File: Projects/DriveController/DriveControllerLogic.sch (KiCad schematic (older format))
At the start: 34 parts, among them U1 ATMega32M1, U2 MCP2562, U3 ATA6844, U4 ACS710

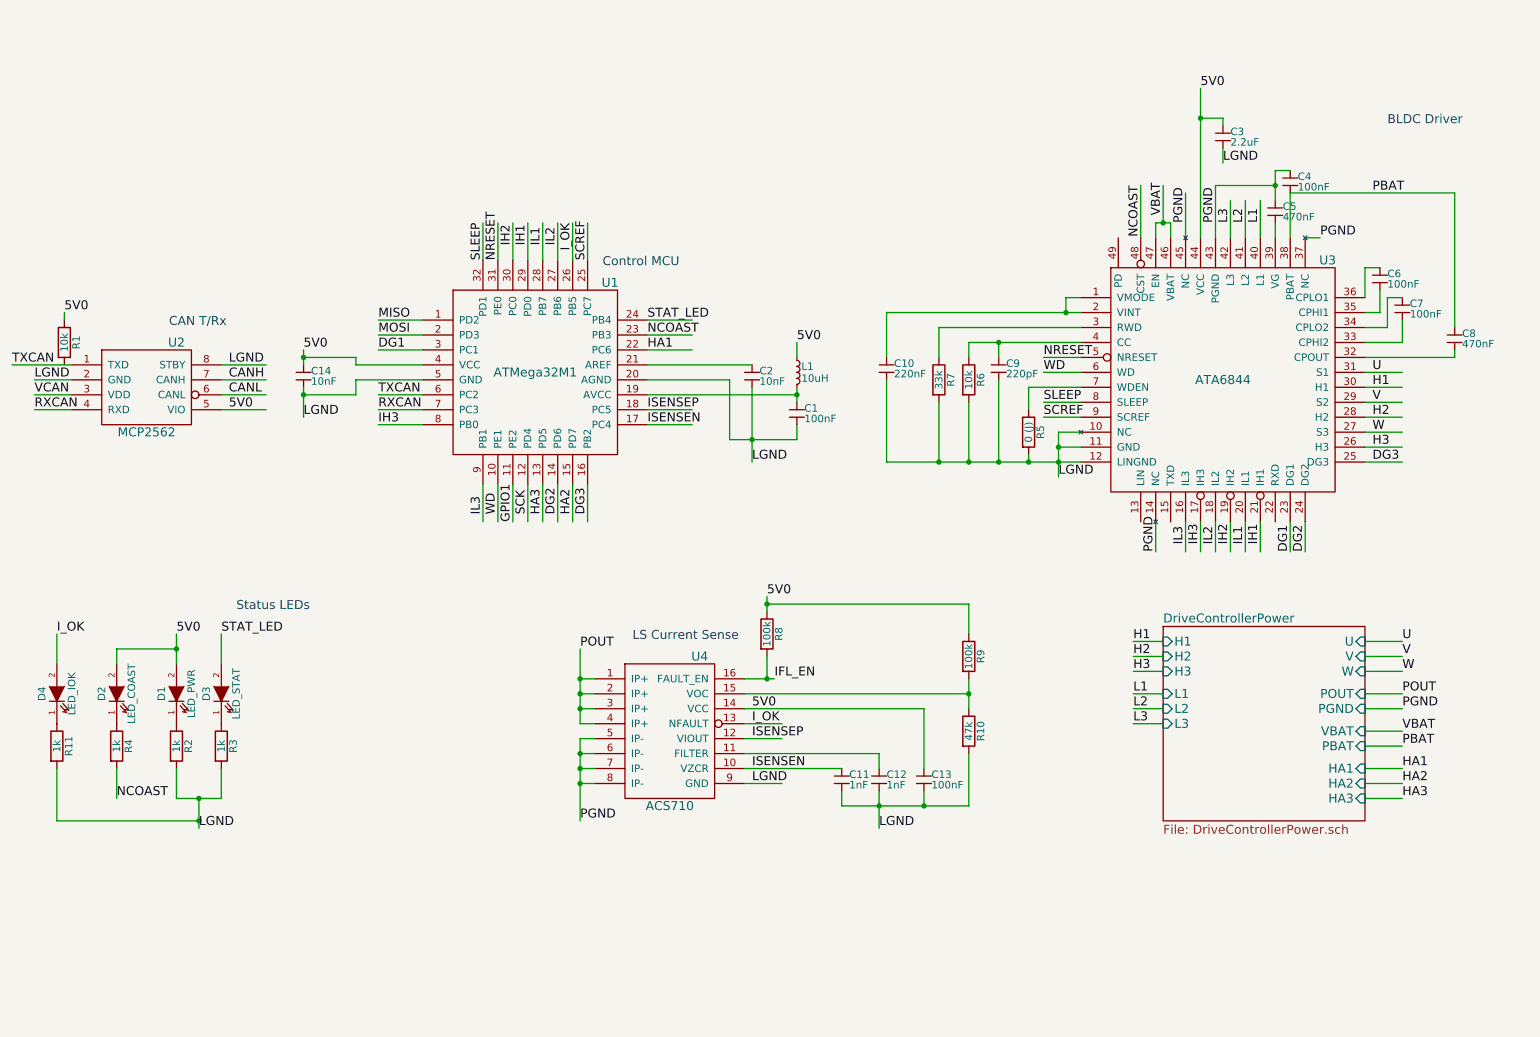
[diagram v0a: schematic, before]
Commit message: Nearly done module schematics
ToDo: Make the footprints for custom parts and layout!
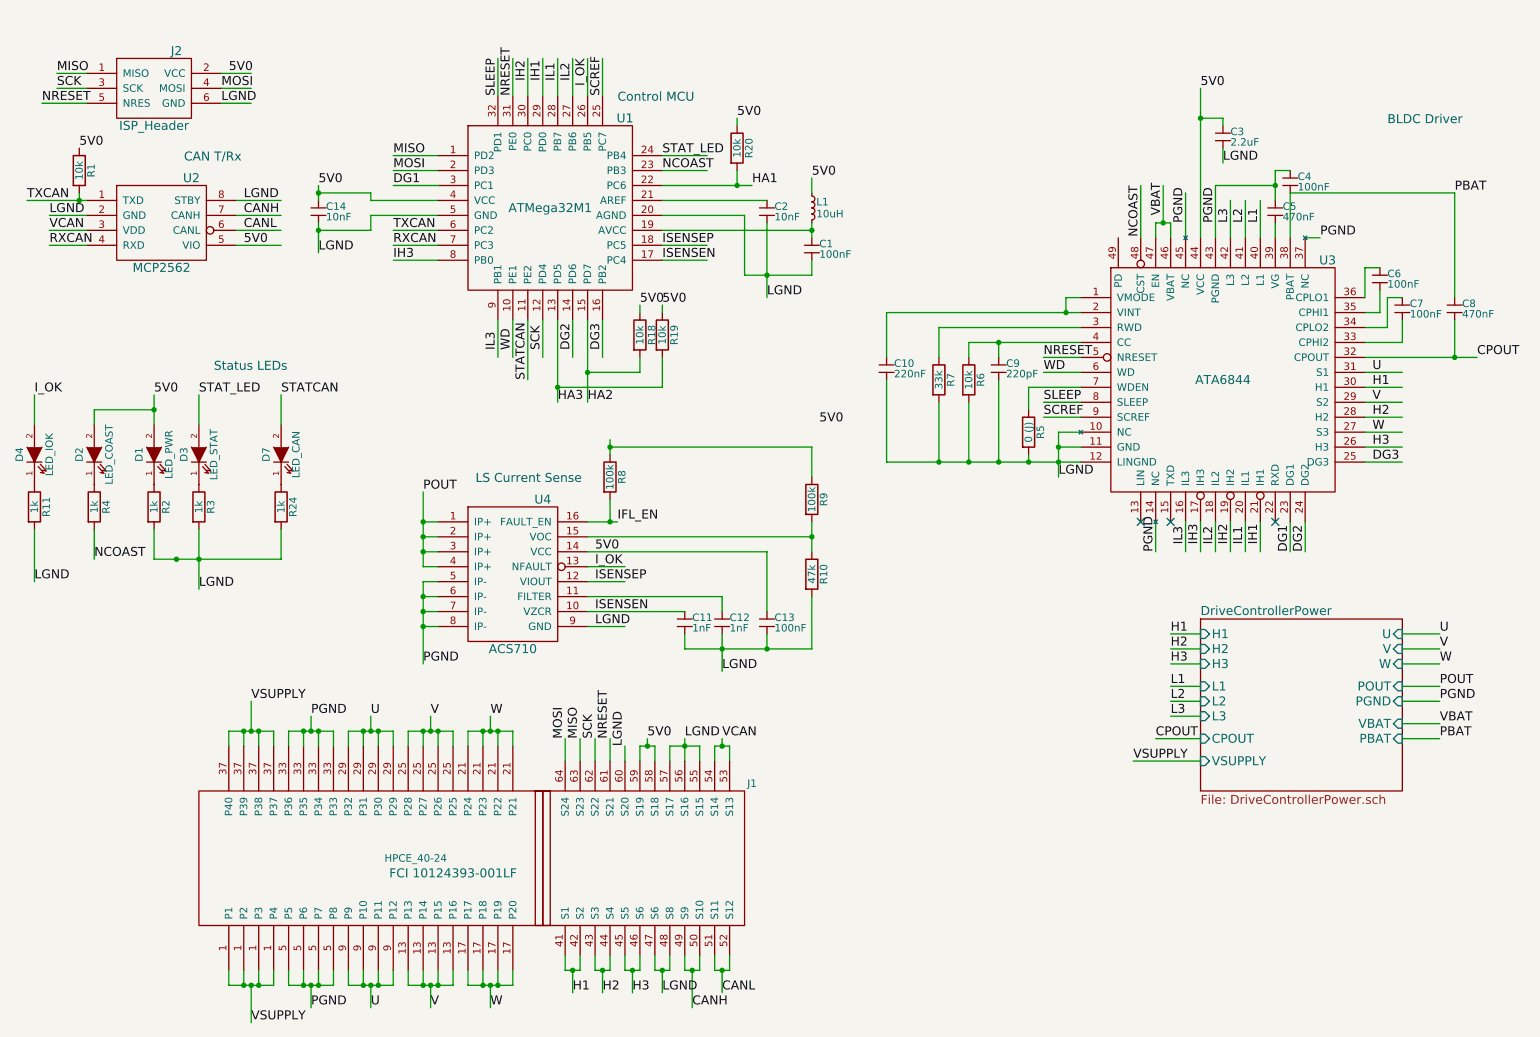
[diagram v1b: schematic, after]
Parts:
- added D7: LED_CAN, symbol LED
- added J1: HPCE_40-24, MODULE, symbol HPCE_40-24
- added J2: ISP_Header, symbol ISP_Header
- added R18, R19, R20: 10k, symbol R
- added R24: 1k, symbol R
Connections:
- net labels added: CPOUT, STATCAN, VSUPPLY
- net labels removed: GPIO1
- wire segments 184 -> 299
- no-connect marks 0 -> 3
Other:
- moved on the sheet: C1, C11, C12, C13, C14, C2, C8, D1, D2, D3, D4, L1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

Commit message: Basic PCB layout organization
No traces yet!
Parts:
- C1, C10, C11, C12, C13, C14, C2, C3, C4, C5, C6, C7, C8, C9, L1: footprint (none) -> Capacitors_SMD:C_0805
- D1, D2, D3, D4, D7: footprint (none) -> LEDs:LED-0805
- J1: footprint MODULE -> USSTPARTS:HPCE-40-24
- J2: footprint (none) -> Pin_Headers:Pin_Header_Straight_2x03
- R1, R10, R11, R18, R19, R2, R20, R24, R3, R4, R5, R6, R7, R8, R9: footprint (none) -> Resistors_SMD:R_0805
- U1: footprint (none) -> Housings_QFP:TQFP-32_7x7mm_Pitch0.8mm
- U2: footprint (none) -> Housings_SOIC:SOIC-8_3.9x4.9mm_Pitch1.27mm
- U3: footprint (none) -> Housings_DFN_QFN:QFN-48-1EP_7x7mm_Pitch0.5mm
- U4: footprint (none) -> Housings_SOIC:SOIC-16_7.5x10.3mm_Pitch1.27mm
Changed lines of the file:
@@
 F 0 "U2" H 1800 2300 60  0000 C CNN
 F 1 "MCP2562" H 1600 1700 60  0000 C CNN
-F 2 "" H 1350 1900 60  0000 C CNN
+F 2 "Housings_SOIC:SOIC-8_3.9x4.9mm_Pitch1.27mm" H 1350 1900 60  0001 C CNN
 F 3 "" H 1350 1900 60  0000 C CNN
 	1    1600 2000
@@
 F 0 "U3" H 9400 3850 60  0000 C CNN
 F 1 "ATA6844" H 8700 3050 60  0000 C CNN
-F 2 "" H 7950 3500 60  0000 C CNN
+F 2 "Housings_DFN_QFN:QFN-48-1EP_7x7mm_Pitch0.5mm" H 7950 3500 60  0001 C CNN
 F 3 "" H 7950 3500 60  0000 C CNN
 	1    8700 3050
@@
 F 0 "U4" H 4150 4850 60  0000 C CNN
 F 1 "ACS710" H 3950 3850 60  0000 C CNN
-F 2 "" H 3650 4350 60  0000 C CNN
+F 2 "Housings_SOIC:SOIC-16_7.5x10.3mm_Pitch1.27mm" H 3650 4350 60  0001 C CNN
 F 3 "" H 3650 4350 60  0000 C CNN
 	1    3950 4350
@@
 F 0 "R1" V 1130 1650 50  0000 C CNN
 F 1 "10k" V 1050 1650 50  0000 C CNN
-F 2 "" V 980 1650 30  0000 C CNN
+F 2 "Resistors_SMD:R_0805" V 980 1650 30  0001 C CNN
 F 3 "" H 1050 1650 30  0000 C CNN
 	1    1050 1650
@@
 F 0 "U1" H 4700 2000 60  0000 C CNN
 F 1 "ATMega32M1" H 4200 1400 60  0000 C CNN
-F 2 "" H 4600 1550 60  0000 C CNN
+F 2 "Housings_QFP:TQFP-32_7x7mm_Pitch0.8mm" H 4600 1550 60  0001 C CNN
 F 3 "" H 4600 1550 60  0000 C CNN
 	1    4500 1650
@@
 F 0 "C2" H 5700 1910 50  0000 L CNN
 F 1 "10nF" H 5700 1840 50  0000 L CNN
-F 2 "" H 5650 1900 60  0000 C CNN
+F 2 "Capacitors_SMD:C_0805" H 5650 1900 60  0001 C CNN
 F 3 "" H 5650 1900 60  0000 C CNN
 	1    5650 1900
@@
 F 0 "C1" H 6000 2160 50  0000 L CNN
 F 1 "100nF" H 6000 2090 50  0000 L CNN
-F 2 "" H 5950 2150 60  0000 C CNN
+F 2 "Capacitors_SMD:C_0805" H 5950 2150 60  0001 C CNN
 F 3 "" H 5950 2150 60  0000 C CNN
 	1    5950 2150
@@
 F 0 "L1" H 5980 1940 50  0000 L CNN
 F 1 "10uH" H 5980 1860 50  0000 L CNN
-F 2 "" H 5950 1900 60  0000 C CNN
+F 2 "Capacitors_SMD:C_0805" H 5950 1900 60  0001 C CNN
 F 3 "" H 5950 1900 60  0000 C CNN
 	1    5950 1900
@@
 F 0 "C14" H 2700 1910 50  0000 L CNN
 F 1 "10nF" H 2700 1840 50  0000 L CNN
-F 2 "" H 2650 1900 60  0000 C CNN
+F 2 "Capacitors_SMD:C_0805" H 2650 1900 60  0001 C CNN
 F 3 "" H 2650 1900 60  0000 C CNN
 	1    2650 1900
@@
 F 0 "D1" H 1550 3650 50  0000 C CNN
 F 1 "LED_PWR" H 1550 3450 50  0000 C CNN
-F 2 "" H 1550 3550 60  0000 C CNN
+F 2 "LEDs:LED-0805" H 1550 3550 60  0001 C CNN
 F 3 "" H 1550 3550 60  0000 C CNN
 	1    1550 3550
@@
 F 0 "D3" H 1850 3650 50  0000 C CNN
 F 1 "LED_STAT" H 1850 3450 50  0000 C CNN
-F 2 "" H 1850 3550 60  0000 C CNN
+F 2 "LEDs:LED-0805" H 1850 3550 60  0001 C CNN
 F 3 "" H 1850 3550 60  0000 C CNN
 	1    1850 3550
@@
 F 0 "R3" V 1930 3900 50  0000 C CNN
 F 1 "1k" V 1850 3900 50  0000 C CNN
-F 2 "" V 1780 3900 30  0000 C CNN
+F 2 "Resistors_SMD:R_0805" V 1780 3900 30  0001 C CNN
 F 3 "" H 1850 3900 30  0000 C CNN
 	1    1850 3900
@@
 F 0 "R2" V 1630 3900 50  0000 C CNN
 F 1 "1k" V 1550 3900 50  0000 C CNN
-F 2 "" V 1480 3900 30  0000 C CNN
+F 2 "Resistors_SMD:R_0805" V 1480 3900 30  0001 C CNN
 F 3 "" H 1550 3900 30  0000 C CNN
 	1    1550 3900
@@
 F 0 "R4" V 1230 3900 50  0000 C CNN
 F 1 "1k" V 1150 3900 50  0000 C CNN
-F 2 "" V 1080 3900 30  0000 C CNN
+F 2 "Resistors_SMD:R_0805" V 1080 3900 30  0001 C CNN
 F 3 "" H 1150 3900 30  0000 C CNN
 	1    1150 3900
@@
 F 0 "D2" H 1150 3650 50  0000 C CNN
 F 1 "LED_COAST" H 1150 3450 50  0000 C CNN
-F 2 "" H 1150 3550 60  0000 C CNN
+F 2 "LEDs:LED-0805" H 1150 3550 60  0001 C CNN
 F 3 "" H 1150 3550 60  0000 C CNN
 	1    1150 3550
@@
 F 0 "C3" H 8750 1410 50  0000 L CNN
 F 1 "2.2uF" H 8750 1340 50  0000 L CNN
-F 2 "" H 8700 1400 60  0000 C CNN
+F 2 "Capacitors_SMD:C_0805" H 8700 1400 60  0001 C CNN
 F 3 "" H 8700 1400 60  0000 C CNN
 	1    8700 1400
@@
 F 0 "C8" H 10300 2560 50  0000 L CNN
 F 1 "470nF" H 10300 2490 50  0000 L CNN
-F 2 "" H 10250 2550 60  0000 C CNN
+F 2 "Capacitors_SMD:C_0805" H 10250 2550 60  0001 C CNN
 F 3 "" H 10250 2550 60  0000 C CNN
 	1    10250 2550
@@
 F 0 "C7" H 9950 2560 50  0000 L CNN
 F 1 "100nF" H 9950 2490 50  0000 L CNN
-F 2 "" H 9900 2550 60  0000 C CNN
+F 2 "Capacitors_SMD:C_0805" H 9900 2550 60  0001 C CNN
 F 3 "" H 9900 2550 60  0000 C CNN
 	1    9900 2550
@@
 F 0 "C6" H 9800 2360 50  0000 L CNN
 F 1 "100nF" H 9800 2290 50  0000 L CNN
-F 2 "" H 9750 2350 60  0000 C CNN
+F 2 "Capacitors_SMD:C_0805" H 9750 2350 60  0001 C CNN
 F 3 "" H 9750 2350 60  0000 C CNN
 	1    9750 2350
@@
 F 0 "C4" H 9200 1710 50  0000 L CNN
 F 1 "100nF" H 9200 1640 50  0000 L CNN
-F 2 "" H 9150 1700 60  0000 C CNN
+F 2 "Capacitors_SMD:C_0805" H 9150 1700 60  0001 C CNN
 F 3 "" H 9150 1700 60  0000 C CNN
 	1    9150 1700
@@
 F 0 "C5" H 9100 1910 50  0000 L CNN
 F 1 "470nF" H 9100 1840 50  0000 L CNN
-F 2 "" H 9050 1900 60  0000 C CNN
+F 2 "Capacitors_SMD:C_0805" H 9050 1900 60  0001 C CNN
 F 3 "" H 9050 1900 60  0000 C CNN
 	1    9050 1900
@@
 F 0 "R5" V 7480 3400 50  0000 C CNN
 F 1 "0 (J)" V 7400 3400 50  0000 C CNN
-F 2 "" V 7330 3400 30  0000 C CNN
+F 2 "Resistors_SMD:R_0805" V 7330 3400 30  0001 C CNN
 F 3 "" H 7400 3400 30  0000 C CNN
 	1    7400 3400
@@
 F 0 "C9" H 7250 2960 50  0000 L CNN
 F 1 "220pF" H 7250 2890 50  0000 L CNN
-F 2 "" H 7200 2950 60  0000 C CNN
+F 2 "Capacitors_SMD:C_0805" H 7200 2950 60  0001 C CNN
 F 3 "" H 7200 2950 60  0000 C CNN
 	1    7200 2950
@@
 F 0 "R6" V 7080 3050 50  0000 C CNN
 F 1 "10k" V 7000 3050 50  0000 C CNN
-F 2 "" V 6930 3050 30  0000 C CNN
+F 2 "Resistors_SMD:R_0805" V 6930 3050 30  0001 C CNN
 F 3 "" H 7000 3050 30  0000 C CNN
 	1    7000 3050
@@
 F 0 "R7" V 6880 3050 50  0000 C CNN
 F 1 "33k" V 6800 3050 50  0000 C CNN
-F 2 "" V 6730 3050 30  0000 C CNN
+F 2 "Resistors_SMD:R_0805" V 6730 3050 30  0001 C CNN
 F 3 "" H 6800 3050 30  0000 C CNN
 	1    6800 3050
@@
 F 0 "C10" H 6500 2960 50  0000 L CNN
 F 1 "220nF" H 6500 2890 50  0000 L CNN
-F 2 "" H 6450 2950 60  0000 C CNN
+F 2 "Capacitors_SMD:C_0805" H 6450 2950 60  0001 C CNN
 F 3 "" H 6450 2950 60  0000 C CNN
 F 4 "ESR:2-15" H 6450 2950 60  0001 C CNN "Note"
@@
 F 0 "R8" V 4680 3700 50  0000 C CNN
 F 1 "100k" V 4600 3700 50  0000 C CNN
-F 2 "" V 4530 3700 30  0000 C CNN
+F 2 "Resistors_SMD:R_0805" V 4530 3700 30  0001 C CNN
 F 3 "" H 4600 3700 30  0000 C CNN
 	1    4600 3700
@@
 F 0 "R9" V 6030 3850 50  0000 C CNN
 F 1 "100k" V 5950 3850 50  0000 C CNN
-F 2 "" V 5880 3850 30  0000 C CNN
+F 2 "Resistors_SMD:R_0805" V 5880 3850 30  0001 C CNN
 F 3 "" H 5950 3850 30  0000 C CNN
 	1    5950 3850
@@
 F 0 "R10" V 6030 4350 50  0000 C CNN
 F 1 "47k" V 5950 4350 50  0000 C CNN
-F 2 "" V 5880 4350 30  0000 C CNN
+F 2 "Resistors_SMD:R_0805" V 5880 4350 30  0001 C CNN
 F 3 "" H 5950 4350 30  0000 C CNN
 	1    5950 4350
@@
 F 0 "C11" H 5150 4660 50  0000 L CNN
 F 1 "1nF" H 5150 4590 50  0000 L CNN
-F 2 "" H 5100 4650 60  0000 C CNN
+F 2 "Capacitors_SMD:C_0805" H 5100 4650 60  0001 C CNN
 F 3 "" H 5100 4650 60  0000 C CNN
 	1    5100 4650
@@
 F 0 "C12" H 5400 4660 50  0000 L CNN
 F 1 "1nF" H 5400 4590 50  0000 L CNN
-F 2 "" H 5350 4650 60  0000 C CNN
+F 2 "Capacitors_SMD:C_0805" H 5350 4650 60  0001 C CNN
 F 3 "" H 5350 4650 60  0000 C CNN
 	1    5350 4650
@@
 F 0 "C13" H 5700 4660 50  0000 L CNN
 F 1 "100nF" H 5700 4590 50  0000 L CNN
-F 2 "" H 5650 4650 60  0000 C CNN
+F 2 "Capacitors_SMD:C_0805" H 5650 4650 60  0001 C CNN
 F 3 "" H 5650 4650 60  0000 C CNN
 	1    5650 4650
@@
 F 0 "D4" H 750 3650 50  0000 C CNN
 F 1 "LED_IOK" H 750 3450 50  0000 C CNN
-F 2 "" H 750 3550 60  0000 C CNN
+F 2 "LEDs:LED-0805" H 750 3550 60  0001 C CNN
 F 3 "" H 750 3550 60  0000 C CNN
 	1    750  3550
@@
 F 0 "R11" V 830 3900 50  0000 C CNN
 F 1 "1k" V 750 3900 50  0000 C CNN
-F 2 "" V 680 3900 30  0000 C CNN
+F 2 "Resistors_SMD:R_0805" V 680 3900 30  0001 C CNN
 F 3 "" H 750 3900 30  0000 C CNN
 	1    750  3900
@@
 F 0 "R18" V 4880 2750 50  0000 C CNN
 F 1 "10k" V 4800 2750 50  0000 C CNN
-F 2 "" V 4730 2750 30  0000 C CNN
+F 2 "Resistors_SMD:R_0805" V 4730 2750 30  0001 C CNN
 F 3 "" H 4800 2750 30  0000 C CNN
 	1    4800 2750
@@
 F 0 "R19" V 5030 2750 50  0000 C CNN
 F 1 "10k" V 4950 2750 50  0000 C CNN
-F 2 "" V 4880 2750 30  0000 C CNN
+F 2 "Resistors_SMD:R_0805" V 4880 2750 30  0001 C CNN
 F 3 "" H 4950 2750 30  0000 C CNN
 	1    4950 2750
@@
 F 0 "R20" V 5530 1500 50  0000 C CNN
 F 1 "10k" V 5450 1500 50  0000 C CNN
-F 2 "" V 5380 1500 30  0000 C CNN
+F 2 "Resistors_SMD:R_0805" V 5380 1500 30  0001 C CNN
 F 3 "" H 5450 1500 30  0000 C CNN
 	1    5450 1500
@@
 F 0 "D7" H 2400 3650 50  0000 C CNN
 F 1 "LED_CAN" H 2400 3450 50  0000 C CNN
-F 2 "" H 2400 3550 60  0000 C CNN
+F 2 "LEDs:LED-0805" H 2400 3550 60  0001 C CNN
 F 3 "" H 2400 3550 60  0000 C CNN
 	1    2400 3550
@@
 F 0 "R24" V 2480 3900 50  0000 C CNN
 F 1 "1k" V 2400 3900 50  0000 C CNN
-F 2 "" V 2330 3900 30  0000 C CNN
+F 2 "Resistors_SMD:R_0805" V 2330 3900 30  0001 C CNN
 F 3 "" H 2400 3900 30  0000 C CNN
 	1    2400 3900
@@
 F 0 "J2" H 1700 1350 60  0000 C CNN
 F 1 "ISP_Header" H 1550 850 60  0000 C CNN
-F 2 "" H 1600 1150 60  0000 C CNN
+F 2 "Pin_Headers:Pin_Header_Straight_2x03" H 1600 1150 60  0001 C CNN
 F 3 "" H 1600 1150 60  0000 C CNN
 	1    1550 1100
@@
 Text Label 5150 7250 0    60   ~ 0
 CANH
-$Comp
-L HPCE_40-24 J1
-U 1 1 56447F0D
-P 3900 6300
-F 0 "J1" H 5550 6850 50  0000 C CNN
-F 1 "HPCE_40-24" H 3300 6350 50  0000 C CNN
-F 2 "MODULE" H 4850 6450 50  0001 C CNN
-F 3 "DOCUMENTATION" H 4850 6300 50  0001 C CNN
-F 4 "FCI 10124393-001LF" H 3550 6250 60  0000 C CNN "Part"
-	1    3900 6300
-	1    0    0    -1
-$EndComp
 Text Label 4750 7150 0    60   ~ 0
 H3
@@
 Text Label 750  4400 0    60   ~ 0
 LGND
+$Comp
+L HPCE_40-24 J1
+U 1 1 56447F0D
+P 3900 6300
+F 0 "J1" H 5550 6850 50  0000 C CNN
+F 1 "HPCE_40-24" H 3300 6350 50  0000 C CNN
+F 2 "USSTPARTS:HPCE-40-24" H 4850 6450 50  0001 C CNN
+F 3 "DOCUMENTATION" H 4850 6300 50  0001 C CNN
+F 4 "FCI 10124393-001LF" H 3550 6250 60  0000 C CNN "Part"
+	1    3900 6300
+	1    0    0    -1
+$EndComp
 $EndSCHEMATC

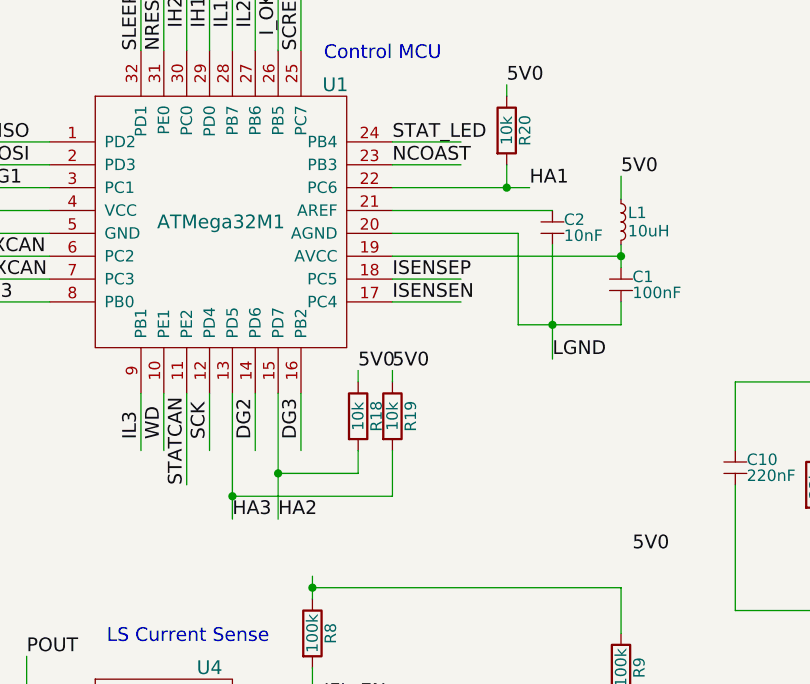
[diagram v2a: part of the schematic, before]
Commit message: More routing
Might start traces over. :page_facing_up:
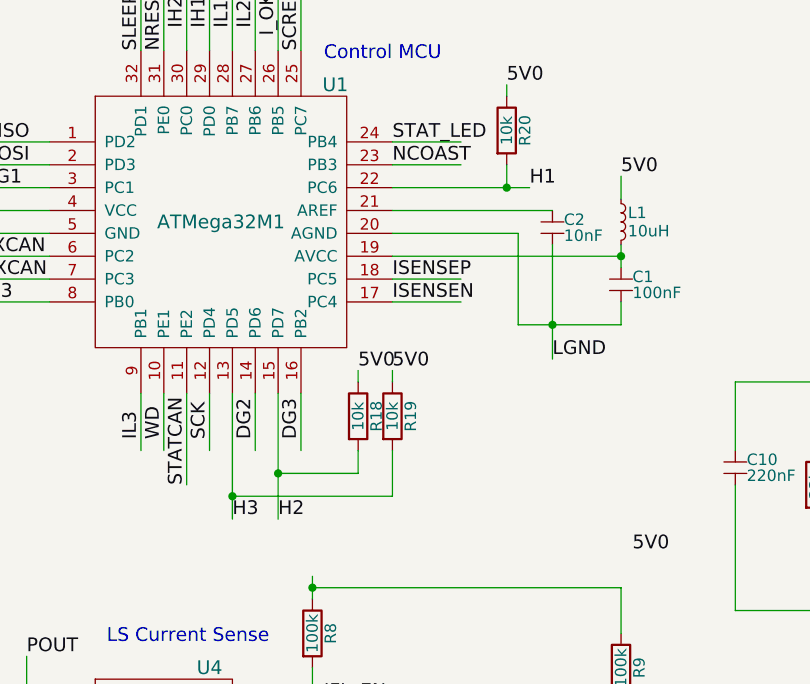
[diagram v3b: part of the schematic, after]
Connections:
- net labels removed: HA1, HA2, HA3
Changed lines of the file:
@@
 ISENSEP
 Text Label 4250 3200 0    60   ~ 0
-HA3
+H3
 Text Label 4450 3200 0    60   ~ 0
-HA2
+H2
 Text Label 5550 1750 0    60   ~ 0
-HA1
+H1
 Text Label 3150 1750 0    60   ~ 0
 DG1
